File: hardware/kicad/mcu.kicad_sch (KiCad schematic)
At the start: 38 parts, among them J101 TC2050-IDC-NL, J102 UART (TX RX GND), SW101 BOOT, U101 STM32F469IIT6, Y101 8MHz CL10pF, Y102 32.768kHz CL6pF

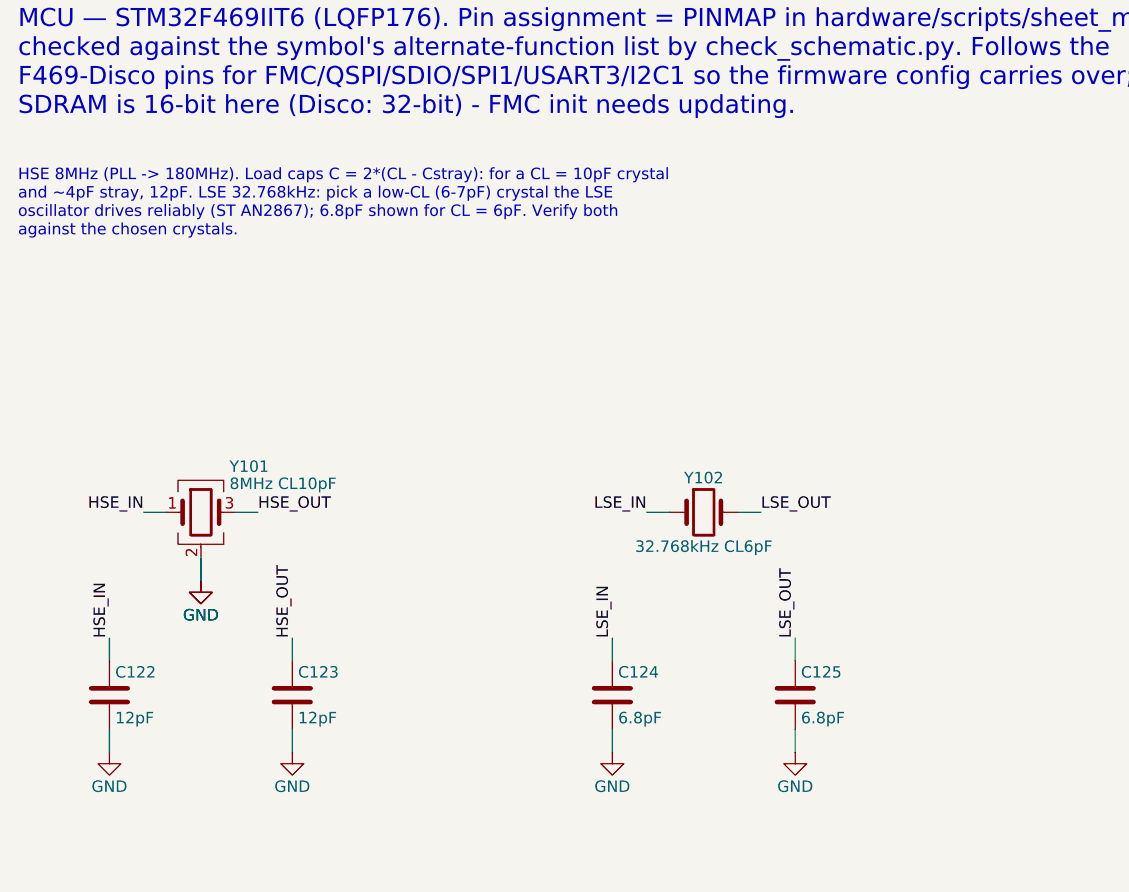
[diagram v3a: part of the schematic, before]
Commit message: Electrode board project, open hardware TODOs, main PCB bootstrap
- hardware/electrode/: side-wall electrode board (one design, two fitted),
  generated by gen_electrode.py (schematic, pad footprint) and
  gen_electrode_pcb.py (board, via KiCad's pcbnew Python) from the
  enclosure's params.py. ERC/DRC/parity clean.
- Datasheet values replace most enclosure placeholders. The encoder is now
  PEC11R-4220F-S0024 (20 mm shaft): the M7 bushing left the 15 mm shaft
  too short for the knob. Knob redesigned around the bushing.
- Schematic: TPD4E05U06 ESD on the electrode lines, HRDY 100k pull-down,
  crystals chosen (NX3225GD 8 MHz / NX3215SA 32.768 kHz) with recomputed
  load caps, all inductors DFE201612E, M2 mounting holes.
- Decisions recorded: USB shield to GND, UVLO restart analysis, soft power
  = STANDBY + WKUP, no fuel gauge on v1, TPS63900 footprint verified.
- Encoder footprint: silkscreen no longer crosses its own lug pads.
- hardware/kicad/stm32-epaper.kicad_pcb: 4-layer board bootstrapped by
  gen_main_pcb.py with the enclosure outline, all footprints and nets, and
  the enclosure-fixed parts placed.

Co-Authored-By: Claude Opus 5.5 <noreply@anthropic.com>
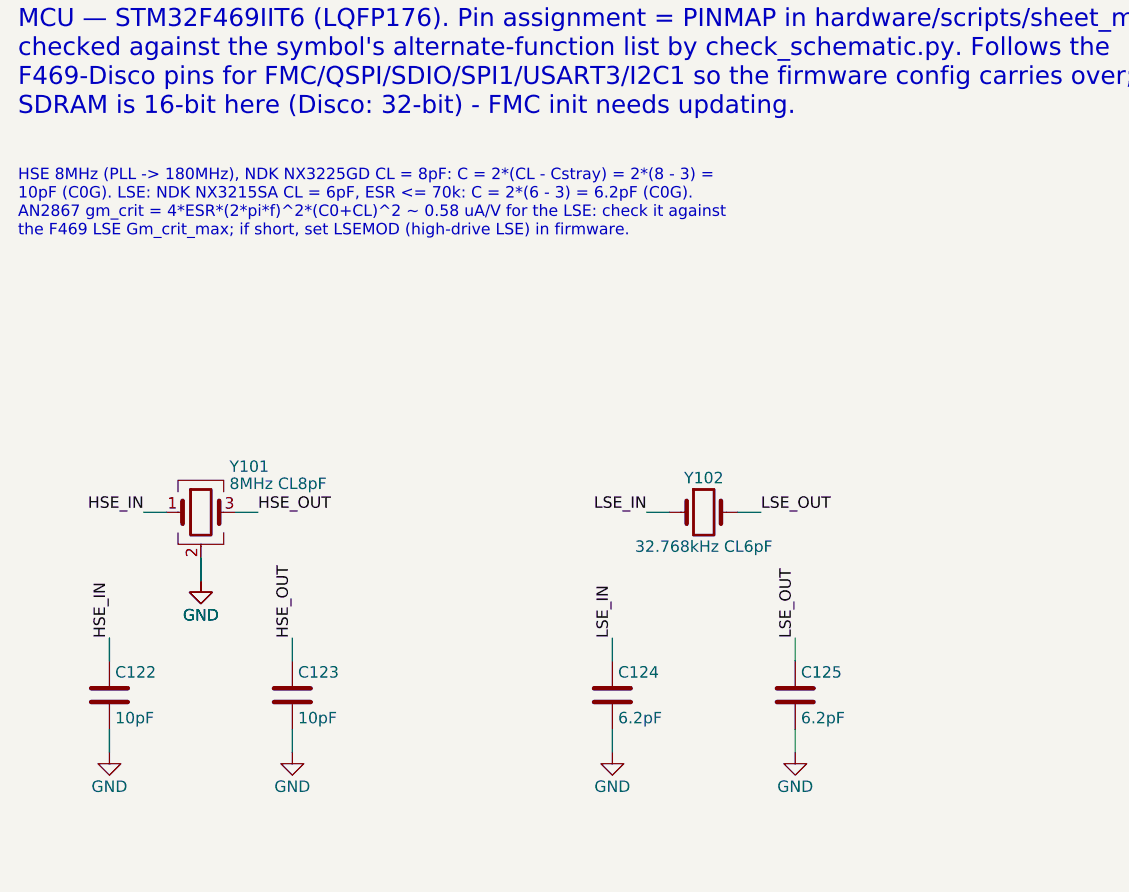
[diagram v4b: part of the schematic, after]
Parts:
- C122, C123: value 12pF -> 10pF
- C124, C125: value 6.8pF -> 6.2pF
- Y101: value 8MHz CL10pF -> 8MHz CL8pF; MPN Abracon ABM8 series, 8MHz, CL=10pF (verify) -> NX3225GD-8MHZ-STD-CRA-3
- Y102: footprint Crystal:Crystal_SMD_2012-2Pin_2.0x1.2mm -> Crystal:Crystal_SMD_3215-2Pin_3.2x1.5mm; MPN 32.768kHz 2012, CL=6pF, low ESR (verify vs AN2867) -> NX3215SA-32.768KHZ-EXS00A-MU00525
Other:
- note added: "HSE 8MHz (PLL -> 180MHz), NDK NX3225GD CL = 8pF: C = 2*(CL - Cstray) = 2*(8 - 3) = 10pF (C0G). LSE: NDK NX3215SA CL = 6pF, ESR <= 70k: C = 2*(6 - 3) = 6.2pF (C0G). AN2867 gm_crit = 4*ESR*(2*pi*f)^2*(C0+CL)^2 ~ 0.58 uA/V for the LSE: check it against the F469 LSE Gm_crit_max; if short, set LSEMOD (high-drive LSE) in firmware."
- note removed: "HSE 8MHz (PLL -> 180MHz). Load caps C = 2*(CL - Cstray): for a CL = 10pF crystal and ~4pF stray, 12pF. LSE 32.768kHz: pick a low-CL (6-7pF) crystal the LSE oscillator drives reliably (ST AN2867); 6.8pF shown for CL = 6pF. Verify both against the chosen crystals."
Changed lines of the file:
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@@
 		)
 	)
-	(text "HSE 8MHz (PLL -> 180MHz). Load caps C = 2*(CL - Cstray): for a CL = 10pF crystal\nand ~4pF stray, 12pF. LSE 32.768kHz: pick a low-CL (6-7pF) crystal the LSE\noscillator drives reliably (ST AN2867); 6.8pF shown for CL = 6pF. Verify both\nagainst the chosen crystals."
+	(text "HSE 8MHz (PLL -> 180MHz), NDK NX3225GD CL = 8pF: C = 2*(CL - Cstray) = 2*(8 - 3) =\n10pF (C0G). LSE: NDK NX3215SA CL = 6pF, ESR <= 70k: C = 2*(6 - 3) = 6.2pF (C0G).\nAN2867 gm_crit = 4*ESR*(2*pi*f)^2*(C0+CL)^2 ~ 0.58 uA/V for the LSE: check it against\nthe F469 LSE Gm_crit_max; if short, set LSEMOD (high-drive LSE) in firmware."
 		(exclude_from_sim no)
 		(at 20.32 30.48 0)
@@
 			)
 		)
-		(property "Value" "8MHz CL10pF"
+		(property "Value" "8MHz CL8pF"
 			(at 43.815 65.405 0)
 			(effects
@@
 			)
 		)
-		(property "MPN" "Abracon ABM8 series, 8MHz, CL=10pF (verify)"
+		(property "MPN" "NX3225GD-8MHZ-STD-CRA-3"
 			(at 40.64 68.58 0)
 			(hide yes)
@@
 			)
 		)
-		(property "Value" "12pF"
+		(property "Value" "10pF"
 			(at 31.115 91.44 0)
 			(effects
@@
 			)
 		)
-		(property "Value" "12pF"
+		(property "Value" "10pF"
 			(at 51.435 91.44 0)
 			(effects
@@
 			)
 		)
-		(property "Footprint" "Crystal:Crystal_SMD_2012-2Pin_2.0x1.2mm"
+		(property "Footprint" "Crystal:Crystal_SMD_3215-2Pin_3.2x1.5mm"
 			(at 96.52 68.58 0)
 			(hide yes)
@@
 			)
 		)
-		(property "MPN" "32.768kHz 2012, CL=6pF, low ESR (verify vs AN2867)"
+		(property "MPN" "NX3215SA-32.768KHZ-EXS00A-MU00525"
 			(at 96.52 68.58 0)
 			(hide yes)
@@
 			)
 		)
-		(property "Value" "6.8pF"
+		(property "Value" "6.2pF"
 			(at 86.995 91.44 0)
 			(effects
@@
 			)
 		)
-		(property "Value" "6.8pF"
+		(property "Value" "6.2pF"
 			(at 107.315 91.44 0)
 			(effects

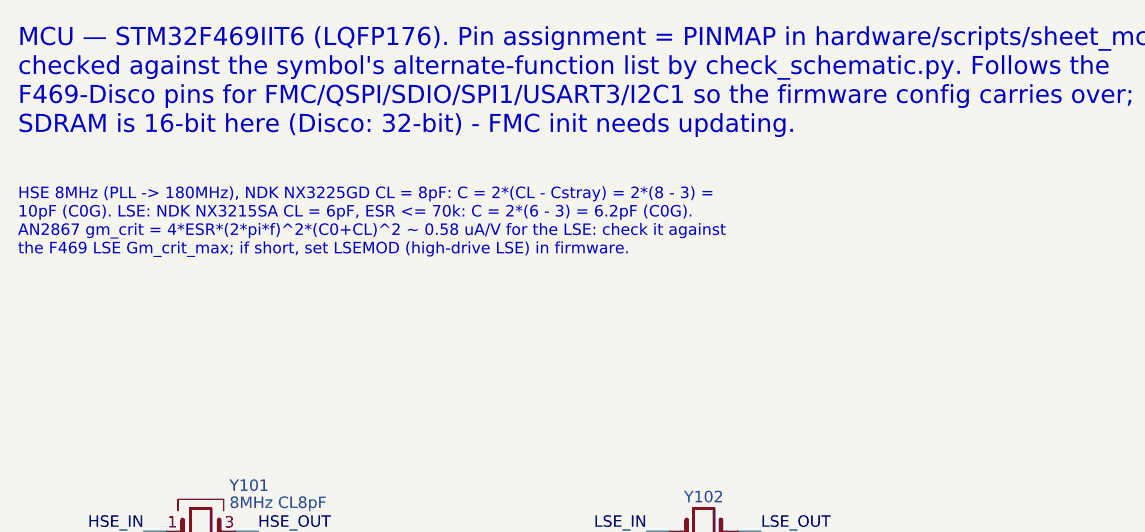
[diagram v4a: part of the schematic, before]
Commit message: Main PCB placement, layout rules, clock terminations, offline freerouting
- place_main_pcb.py: hand floorplan for the ICs plus a greedy placer
  (parts next to what they connect to, decoupling at their IC's power
  pins, clock series resistors at their MCU pins), inner planes
  In1 = GND / In2 = +3V3. CAP1188 moved top-middle between J302/J303.
- Net classes (Power, Rail3V3, Touch, Clock) set by gen_main_pcb.py and
  exported to the router; stm32-epaper.kicad_dru adds length/skew limits
  for the SDRAM/SDIO/QSPI buses, USB pair, crystals and touch lines,
  checked by KiCad DRC after routing.
- Schematic: 22/33R source series resistors R208-R210 on the SDRAM,
  microSD and QSPI clocks; check_schematic.py verifies they bridge the
  right nets.
- route_main_pcb.py: Specctra DSN/SES round trip for headless freerouting.
- .mcp.json: freerouting MCP server switched to the local jar (offline, no
  API key).
- docs/DS_stm32f469ae.pdf added; LSE margin checked (needs high-drive mode).
- Enclosure: fit-check print export (chin section + knob) and checklist.

Co-Authored-By: Claude Opus 5.5 <noreply@anthropic.com>
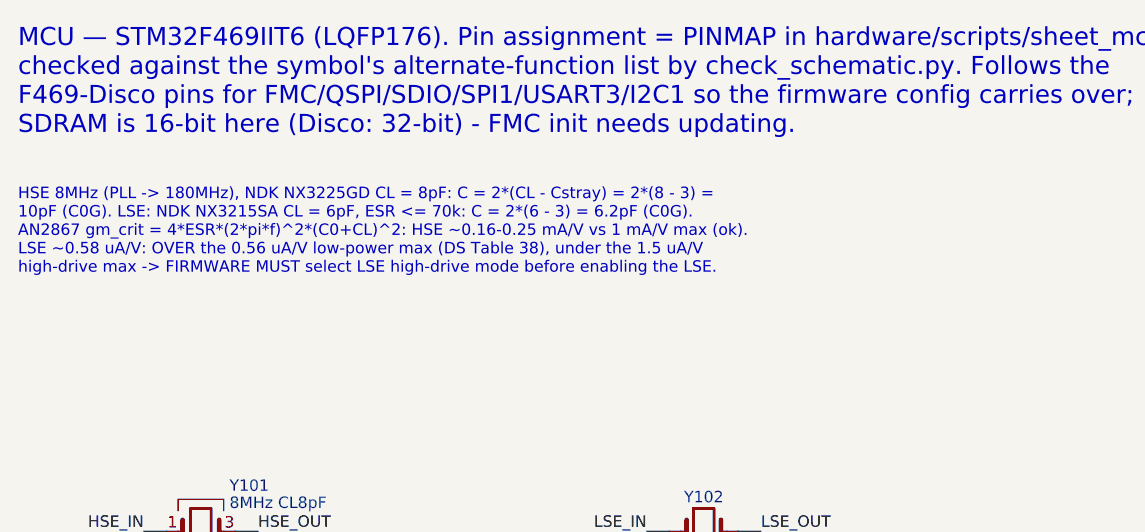
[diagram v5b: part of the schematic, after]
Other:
- note added: "HSE 8MHz (PLL -> 180MHz), NDK NX3225GD CL = 8pF: C = 2*(CL - Cstray) = 2*(8 - 3) = 10pF (C0G). LSE: NDK NX3215SA CL = 6pF, ESR <= 70k: C = 2*(6 - 3) = 6.2pF (C0G). AN2867 gm_crit = 4*ESR*(2*pi*f)^2*(C0+CL)^2: HSE ~0.16-0.25 mA/V vs 1 mA/V max (ok). LSE ~0.58 uA/V: OVER the 0.56 uA/V low-power max (DS Table 38), under the 1.5 uA/V high-drive max -> FIRMWARE MUST select LSE high-drive mode before e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"
- note removed: "HSE 8MHz (PLL -> 180MHz), NDK NX3225GD CL = 8pF: C = 2*(CL - Cstray) = 2*(8 - 3) = 10pF (C0G). LSE: NDK NX3215SA CL = 6pF, ESR <= 70k: C = 2*(6 - 3) = 6.2pF (C0G). AN2867 gm_crit = 4*ESR*(2*pi*f)^2*(C0+CL)^2 ~ 0.58 uA/V for the LSE: check it against the F469 LSE Gm_crit_max; if short, set LSEMOD (high-drive LSE) in firmware."
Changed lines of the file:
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@@
 		)
 	)
-	(text "HSE 8MHz (PLL -> 180MHz), NDK NX3225GD CL = 8pF: C = 2*(CL - Cstray) = 2*(8 - 3) =\n10pF (C0G). LSE: NDK NX3215SA CL = 6pF, ESR <= 70k: C = 2*(6 - 3) = 6.2pF (C0G).\nAN2867 gm_crit = 4*ESR*(2*pi*f)^2*(C0+CL)^2 ~ 0.58 uA/V for the LSE: check it against\nthe F469 LSE Gm_crit_max; if short, set LSEMOD (high-drive LSE) in firmware."
+	(text "HSE 8MHz (PLL -> 180MHz), NDK NX3225GD CL = 8pF: C = 2*(CL - Cstray) = 2*(8 - 3) =\n10pF (C0G). LSE: NDK NX3215SA CL = 6pF, ESR <= 70k: C = 2*(6 - 3) = 6.2pF (C0G).\nAN2867 gm_crit = 4*ESR*(2*pi*f)^2*(C0+CL)^2: HSE ~0.16-0.25 mA/V vs 1 mA/V max (ok).\nLSE ~0.58 uA/V: OVER the 0.56 uA/V low-power max (DS Table 38), under the 1.5 uA/V\nhigh-drive max -> FIRMWARE MUST select LSE high-drive mode before enabling the LSE."
 		(exclude_from_sim no)
 		(at 20.32 30.48 0)

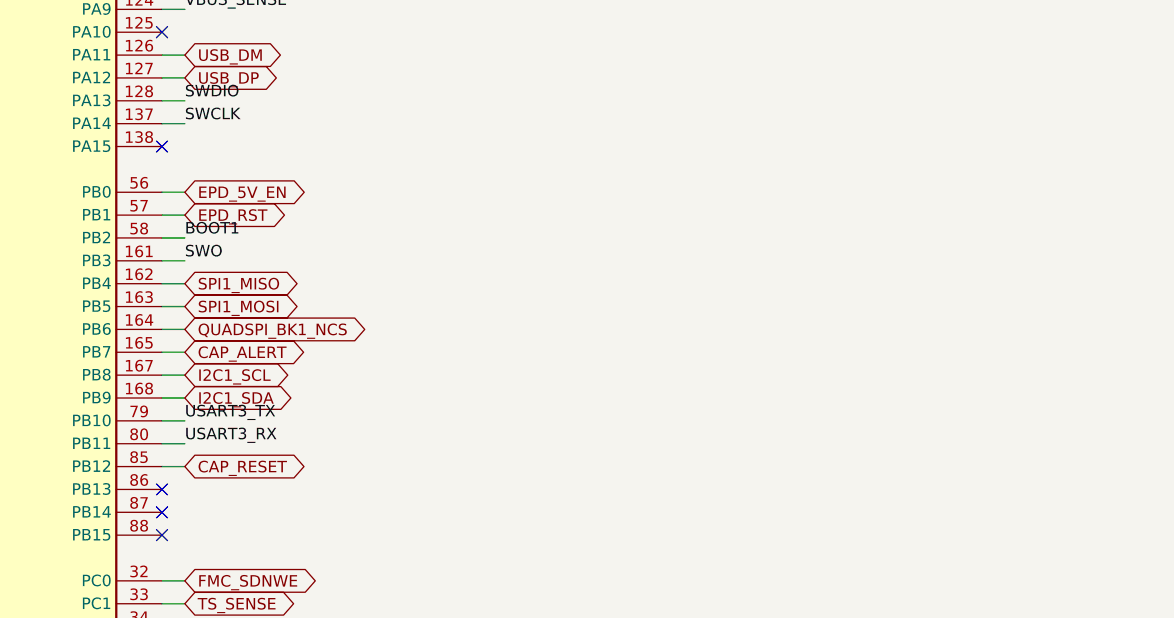
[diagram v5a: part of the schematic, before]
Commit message: Board: Michael's routing in KiCad (0 unconnected); schematic pilot: I2C pull-ups wired on the MCU sheet
- stm32-epaper.kicad_pcb as saved from KiCad 2026-09-24 07:39 (last two
  connections routed by hand: DRC 0 unconnected), footprints re-linked to the
  redrawn schematic (R304/R305 -> R105/R106) by sync_board_to_schematic.py.
- Schematic pilot: I2C1 pull-ups drawn wired to PB8/PB9 with junctions
  (moved from the Peripherals sheet). compare_netlists.py: electrically
  identical (156 parts, 193 nets).

Co-Authored-By: Claude Opus 5.5 <noreply@anthropic.com>
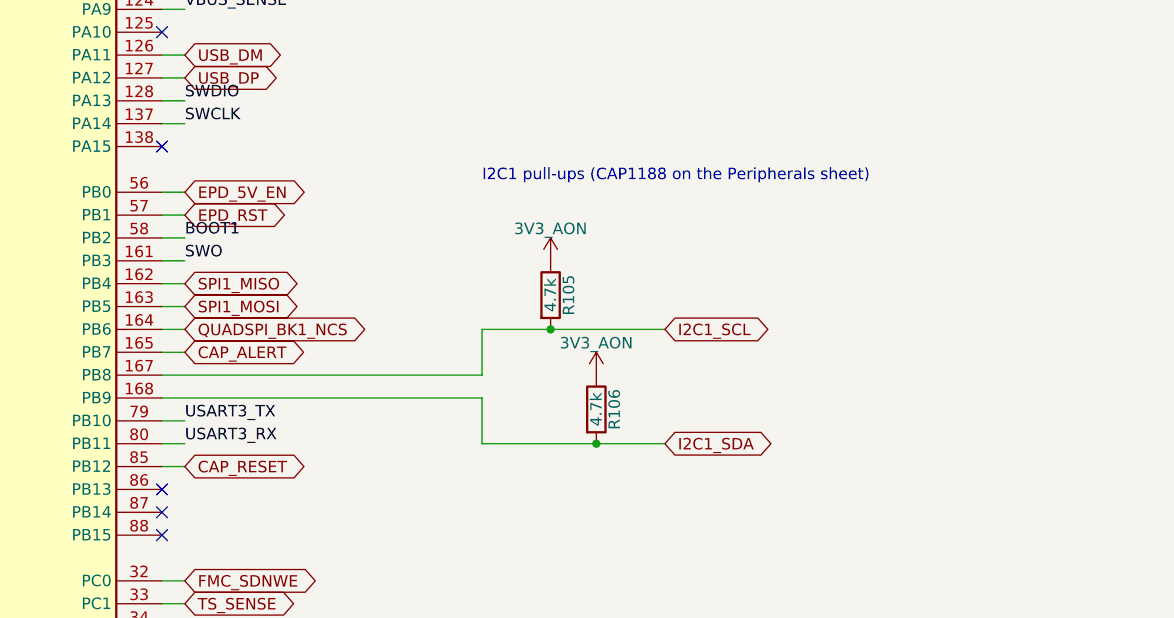
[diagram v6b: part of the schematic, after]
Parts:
- removed C114: 4.7uF, Capacitor_SMD:C_0603_1608Metric, symbol Device:C
- removed J102: UART (TX RX GND), Connector_PinHeader_1.27mm:PinHeader_1x03_P1.27mm_Vertical, symbol Connector_Generic:Conn_01x03
- added C101: 100nF, Capacitor_SMD:C_0402_1005Metric, symbol Device:C
- added FB101: BLM18PG221SN1, Inductor_SMD:L_0603_1608Metric, symbol Device:FerriteBead_Small
- added R103: 1k, Resistor_SMD:R_0402_1005Metric, symbol Device:R
- added R106: 4.7k, Resistor_SMD:R_0402_1005Metric, symbol Device:R
- C114: renamed from FB101; value BLM18PG221SN1 -> 4.7uF; footprint Inductor_SMD:L_0603_1608Metric -> Capacitor_SMD:C_0603_1608Metric; symbol Device:FerriteBead_Small -> Device:C
- J102: renamed from R103; value 1k -> UART (TX RX GND); footprint Resistor_SMD:R_0402_1005Metric -> Connector_PinHeader_1.27mm:PinHeader_1x03_P1.27mm_Vertical; symbol Device:R -> Connector_Generic:Conn_01x03
- R105: renamed from C101; value 100nF -> 4.7k; footprint Capacitor_SMD:C_0402_1005Metric -> Resistor_SMD:R_0402_1005Metric; symbol Device:C -> Device:R
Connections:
- net 3V3_AON: now also C101.1, FB101.1, R106.1
- net GND: now also C114.2, J102.3 (Pin_3), C101.2; no longer R105.2
- net I2C1_SCL: now also R105.2
- net I2C1_SDA: now also R106.2
- net LED1_A: now also R103.2; no longer J102.2
- net LED_STATUS: now also R103.1; no longer J102.1
- net USART3_RX: now also J102.2 (Pin_2)
- net USART3_TX: now also J102.1 (Pin_1)
- net VDDA: now also FB101.2; no longer C114.2
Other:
- note added: "I2C1 pull-ups (CAP1188 on the Peripherals sheet)"

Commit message: Schematic: MCU sheet redrawn with wired circuits
VDD pins on one 3V3_AON rail with the decoupling bank, VDDUSB/VDDDSI rail +
C115, VDDA rail through FB101 with its caps and PWR_FLAG, VCAP caps, both
crystals with load caps, BOOT1/VBUS_SENSE/status LED and I2C pull-ups wired
to their pins, BYPASS_REG into the GND rail. Reset/BOOT0 stay label-joined
(boxed in between power pins) but are wired blocks. New wiring.py helpers,
rotated parts in kicad_gen. compare_netlists: electrically identical; board
re-synced (0 unconnected, 0 parity issues).

Co-Authored-By: Claude Opus 5.5 <noreply@anthropic.com>
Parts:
- removed R105: 4.7k, Resistor_SMD:R_0402_1005Metric, symbol Device:R
- removed Y102: 32.768kHz CL6pF, Crystal:Crystal_SMD_3215-2Pin_3.2x1.5mm, symbol Device:Crystal
- added C117: 100nF, Capacitor_SMD:C_0402_1005Metric, symbol Device:C
- added C120: 2.2uF, Capacitor_SMD:C_0402_1005Metric, symbol Device:C
- R105: renamed from C120; value 2.2uF -> 4.7k; footprint Capacitor_SMD:C_0402_1005Metric -> Resistor_SMD:R_0402_1005Metric; symbol Device:C -> Device:R; Note ESR < 2 ohm -> (none)
- Y102: renamed from C117; value 100nF -> 32.768kHz CL6pF; footprint Capacitor_SMD:C_0402_1005Metric -> Crystal:Crystal_SMD_3215-2Pin_3.2x1.5mm; symbol Device:C -> Device:Crystal; MPN (none) -> NX3215SA-32.768KHZ-EXS00A-MU00525
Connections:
- net 3V3_AON: now also R105.1
- net GND: now also C117.2, C120.2; no longer R105.2, Y102.2
- net I2C1_SCL: now also R105.2
- net LSE_IN: now also Y102.1
- net LSE_OUT: now also Y102.2
- net VCAP1: now also C120.1; no longer R105.1
- net VDDA: now also C117.1; no longer Y102.1
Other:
- note added: "Decoupling (DS11189 Fig. 24): 100nF per VDD pin + 4.7uF; place each 100nF at its pin"
- note added: "Reset: 100nF on NRST (internal pull-up). BOOT0 10k pull-down + BOOT button to 3V3: hold BOOT while resetting (or plugging USB) to enter the ROM USB DFU bootloader. PB2 = BOOT1 pulled low (R102, by the MCU) so BOOT0=1 selects system memory."
- note added: "VDDA / VREF+: FB101 + 2 x (1uF + 100nF)"
- note removed: "Decoupling per DS11189 Fig. 24: 100nF on each of the 13 VDD pins + 4.7uF; 100nF on VDDUSB; VDDA and VREF+ (tied, fed through FB101) 1uF + 100nF each; VCAP1/VCAP2 2.2uF (ESR < 2 ohm). Place each 100nF at its pin. VDD12DSI/VCAPDSI: no cap (DSI unused)."
- note removed: "Reset: 100nF on NRST (internal pull-up). BOOT0 10k pull-down + BOOT button to 3V3: hold BOOT while resetting (or plugging USB) to enter the ROM USB DFU bootloader. PB2 = BOOT1 pulled low so BOOT0=1 selects system memory."
